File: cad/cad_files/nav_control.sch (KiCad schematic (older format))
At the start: 10 parts

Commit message: Adding refdes details for nav_control
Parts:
- gave numbers to parts that had none: 10
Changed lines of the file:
@@
-EESchema Schematic File Version 2  date Wed 03 Dec 2014 01:00:34 PM HST
+EESchema Schematic File Version 2  date Wed 03 Dec 2014 04:59:28 PM HST
 LIBS:local_parts
 LIBS:power
@@
 Sheet 2 4
 Title ""
-Date "3 dec 2014"
+Date "4 dec 2014"
 Rev ""
 Comp ""
@@
 charge_status
 $Comp
-L ARDUINO_PRO_MINI U?
+L ARDUINO_PRO_MINI Uc101
 U 1 1 547EB67E
 P 3000 5000
-F 0 "U?" H 3000 4900 50  0000 C CNN
+F 0 "Uc101" H 3000 4900 50  0000 C CNN
 F 1 "ARDUINO_PRO_MINI" V 3100 5350 50  0000 C CNN
 F 2 "MODULE" H 3000 5000 50  0001 C CNN
@@
 $EndComp
 $Comp
-L R R?
+L R Rc101
 U 1 1 547E9539
 P 2900 3550
-F 0 "R?" V 2980 3550 50  0000 C CNN
+F 0 "Rc101" V 2980 3550 50  0000 C CNN
 F 1 "DNP" V 2900 3550 50  0000 C CNN
 	1    2900 3550
@@
 for power switching \nbypass (always on)
 $Comp
-L R R?
+L R Rp303
 U 1 1 547C6270
 P 5100 1800
-F 0 "R?" V 5180 1800 50  0000 C CNN
+F 0 "Rp303" V 5180 1800 50  0000 C CNN
 F 1 "DNP" V 5100 1800 50  0000 C CNN
 	1    5100 1800
@@
 header for power supply \n(boost  to 3.3 or 5 V)\ncheck rotation...
 $Comp
-L CONN_3 K?
+L CONN_3 Kp301
 U 1 1 546DDB52
 P 6350 2500
-F 0 "K?" V 6300 2500 50  0000 C CNN
+F 0 "Kp301" V 6300 2500 50  0000 C CNN
 F 1 "CONN_3" V 6400 2500 40  0000 C CNN
 	1    6350 2500
@@
 Vppath
 $Comp
-L MOSFET_P Q?
+L MOSFET_P Qp301
 U 1 1 53D1B1AA
 P 4700 1800
-F 0 "Q?" H 4700 1990 60  0000 R CNN
+F 0 "Qp301" H 4700 1990 60  0000 R CNN
 F 1 "MOSFET_P" H 4700 1620 60  0000 R CNN
 	1    4700 1800
@@
 $EndComp
 $Comp
-L DIODE D?
+L DIODE Dp301
 U 1 1 53D1B1A5
 P 3700 1200
-F 0 "D?" H 3700 1300 40  0000 C CNN
+F 0 "Dp301" H 3700 1300 40  0000 C CNN
 F 1 "DIODE" H 3700 1100 40  0000 C CNN
 	1    3700 1200
@@
 $EndComp
 $Comp
-L DIODE D?
+L DIODE Dp302
 U 1 1 53D1B19F
 P 3700 1600
-F 0 "D?" H 3700 1700 40  0000 C CNN
+F 0 "Dp302" H 3700 1700 40  0000 C CNN
 F 1 "DIODE" H 3700 1500 40  0000 C CNN
 	1    3700 1600
@@
 $EndComp
 $Comp
-L R R?
+L R Rp302
 U 1 1 53D1B197
 P 4100 2250
-F 0 "R?" V 4180 2250 50  0000 C CNN
+F 0 "Rp302" V 4180 2250 50  0000 C CNN
 F 1 "R" V 4100 2250 50  0000 C CNN
 	1    4100 2250
@@
 $EndComp
 $Comp
-L R R?
+L R Rp301
 U 1 1 53D1B192
 P 3300 2250
-F 0 "R?" V 3380 2250 50  0000 C CNN
+F 0 "Rp301" V 3380 2250 50  0000 C CNN
 F 1 "R" V 3300 2250 50  0000 C CNN
 	1    3300 2250
@@
 $EndComp
 $Comp
-L SW_PUSH SW?
+L SW_PUSH SWp301
 U 1 1 53D1B188
 P 2800 1800
-F 0 "SW?" H 2950 1910 50  0000 C CNN
+F 0 "SWp301" H 2950 1910 50  0000 C CNN
 F 1 "SW_PUSH" H 2800 1720 50  0000 C CNN
 	1    2800 1800

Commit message: Changing transistor to load switch for soft power
FPF2103 or a related model
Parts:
- removed Qp301: MOSFET_P, symbol MOSFET_P
- added Up301: FPF2100, symbol FPF2100
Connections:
- net labels added: PWR_FAULT
- wire segments 39 -> 45
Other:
- moved on the sheet: Kp301, Rp303
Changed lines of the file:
@@
-EESchema Schematic File Version 2  date Wed 03 Dec 2014 04:59:28 PM HST
+EESchema Schematic File Version 2  date Wed 03 Dec 2014 05:34:03 PM HST
 LIBS:local_parts
 LIBS:power
@@
 Comment4 ""
 $EndDescr
-Connection ~ 5900 2200
-Wire Wire Line
-	5900 2200 5900 2400
+Wire Wire Line
+	5500 2600 5600 2600
+Wire Wire Line
+	4500 2500 4500 2400
+Wire Wire Line
+	4500 2400 4600 2400
+Wire Wire Line
+	4600 2600 4300 2600
+Wire Wire Line
+	4300 2600 4300 1800
+Connection ~ 6200 2200
+Wire Wire Line
+	6200 2200 6200 2000
+Wire Wire Line
+	3800 4800 4000 4800
+Wire Wire Line
+	3800 4500 4000 4500
+Connection ~ 3100 6200
+Wire Wire Line
+	3100 6200 3200 6200
+Wire Wire Line
+	3200 6200 3200 6100
+Wire Wire Line
+	2700 3300 2700 3900
+Wire Wire Line
+	2900 3200 2900 3300
+Wire Wire Line
+	6500 2500 6200 2500
+Wire Wire Line
+	6200 2500 6200 2400
+Connection ~ 2300 1000
+Wire Wire Line
+	2500 1000 5600 1000
+Connection ~ 5600 2200
+Wire Wire Line
+	5600 2050 5600 2200
+Wire Wire Line
+	4100 2700 4100 2500
+Wire Wire Line
+	2500 1800 2300 1800
+Wire Wire Line
+	2300 1800 2300 1000
+Connection ~ 4100 1800
+Wire Wire Line
+	4300 1800 4100 1800
+Wire Wire Line
+	3300 1200 3500 1200
+Connection ~ 3300 1600
+Wire Wire Line
+	3500 1600 3300 1600
+Wire Wire Line
+	3300 2000 3300 1400
+Wire Wire Line
+	3100 1800 3300 1800
+Connection ~ 3300 1800
+Wire Wire Line
+	3900 1600 4100 1600
+Wire Wire Line
+	3900 1200 4100 1200
+Wire Wire Line
+	4100 1200 4100 2000
+Connection ~ 4100 1600
+Wire Wire Line
+	4500 1000 4500 2200
+Wire Wire Line
+	3300 2500 3300 2600
+Wire Wire Line
+	3300 2600 4100 2600
+Connection ~ 4100 2600
+Wire Wire Line
+	5600 1000 5600 1550
+Connection ~ 4500 1000
+Wire Wire Line
+	2000 1100 2200 1100
+Wire Wire Line
+	2200 1100 2200 1300
+Wire Wire Line
+	7100 2200 5500 2200
+Wire Wire Line
+	6500 2400 6400 2400
+Wire Wire Line
+	6500 2600 6400 2600
+Wire Wire Line
+	6400 2600 6400 2700
+Wire Wire Line
+	2900 3900 2900 3800
+Wire Wire Line
+	3100 6100 3100 6300
+Wire Wire Line
+	3800 4400 4000 4400
+Wire Wire Line
+	3800 4600 4000 4600
 Wire Wire Line
 	3800 4900 4000 4900
 Wire Wire Line
-	3800 4600 4000 4600
-Wire Wire Line
-	3800 4400 4000 4400
-Wire Wire Line
-	3100 6100 3100 6300
-Wire Wire Line
-	2900 3900 2900 3800
-Wire Wire Line
-	5900 2700 5900 2600
-Wire Wire Line
-	5900 2600 6000 2600
-Wire Wire Line
-	5900 2400 6000 2400
-Wire Wire Line
-	6600 2200 4800 2200
-Wire Wire Line
-	2200 1300 2200 1100
-Wire Wire Line
-	2200 1100 2000 1100
-Connection ~ 4800 1000
-Wire Wire Line
-	5100 1550 5100 1000
-Connection ~ 4100 2600
-Wire Wire Line
-	4100 2600 3300 2600
-Wire Wire Line
-	3300 2600 3300 2500
-Wire Wire Line
-	4800 1600 4800 1000
-Wire Wire Line
-	4800 2200 4800 2000
-Connection ~ 4100 1600
-Wire Wire Line
-	4100 2000 4100 1200
-Wire Wire Line
-	4100 1200 3900 1200
-Wire Wire Line
-	3900 1600 4100 1600
-Connection ~ 3300 1800
-Wire Wire Line
-	3100 1800 3300 1800
-Wire Wire Line
-	3300 2000 3300 1400
-Wire Wire Line
-	3300 1600 3500 1600
-Connection ~ 3300 1600
-Wire Wire Line
-	3300 1200 3500 1200
-Wire Wire Line
-	4100 1800 4500 1800
-Connection ~ 4100 1800
-Wire Wire Line
-	2300 1000 2300 1800
-Wire Wire Line
-	2300 1800 2500 1800
-Wire Wire Line
-	4100 2700 4100 2500
-Wire Wire Line
-	5100 2050 5100 2200
-Connection ~ 5100 2200
-Wire Wire Line
-	5100 1000 2000 1000
-Connection ~ 2300 1000
-Wire Wire Line
-	5700 2400 5700 2500
-Wire Wire Line
-	5700 2500 6000 2500
-Wire Wire Line
-	2900 3200 2900 3300
-Wire Wire Line
-	2700 3300 2700 3900
-Wire Wire Line
-	3200 6100 3200 6200
-Wire Wire Line
-	3200 6200 3100 6200
-Connection ~ 3100 6200
-Wire Wire Line
-	3800 4500 4000 4500
-Wire Wire Line
-	3800 4800 4000 4800
-Wire Wire Line
-	5700 2000 5700 2200
-Connection ~ 5700 2200
+	6400 2400 6400 2200
+Connection ~ 6400 2200
+Wire Wire Line
+	4500 2200 4600 2200
+Wire Wire Line
+	3800 5000 4000 5000
+Text Label 5600 2600 0    60   ~ 0
+PWR_FAULT
+Text Label 4000 5000 0    60   ~ 0
+PWR_FAULT
+$Comp
+L GND #PWR?
+U 1 1 547FD4F0
+P 4500 2500
+F 0 "#PWR?" H 4500 2500 30  0001 C CNN
+F 1 "GND" H 4500 2430 30  0001 C CNN
+	1    4500 2500
+	1    0    0    -1
+$EndComp
+$Comp
+L FPF2100 Up301
+U 1 1 547FD495
+P 5050 2400
+F 0 "Up301" H 5050 2300 60  0000 C CNN
+F 1 "FPF2100" H 5050 2500 60  0000 C CNN
+	1    5050 2400
+	1    0    0    -1
+$EndComp
 Text Notes 4900 4800 0    60   ~ 0
 P6 to turn on LED (PWM: 3, 5, 6, 9, 10, 11)\nP7 to turn on  power (when running with a soft switch)
@@
 L +5V #PWR?
 U 1 1 547E62DF
-P 5700 2400
-F 0 "#PWR?" H 5700 2490 20  0001 C CNN
-F 1 "+5V" H 5700 2490 30  0000 C CNN
-	1    5700 2400
+P 6200 2400
+F 0 "#PWR?" H 6200 2490 20  0001 C CNN
+F 1 "+5V" H 6200 2490 30  0000 C CNN
+	1    6200 2400
 	1    0    0    -1
 $EndComp
@@
 L GND #PWR?
 U 1 1 547E62B9
-P 5900 2700
-F 0 "#PWR?" H 5900 2700 30  0001 C CNN
-F 1 "GND" H 5900 2630 30  0001 C CNN
-	1    5900 2700
+P 6400 2700
+F 0 "#PWR?" H 6400 2700 30  0001 C CNN
+F 1 "GND" H 6400 2630 30  0001 C CNN
+	1    6400 2700
 	1    0    0    -1
 $EndComp
@@
 	1    0    0    -1
 $EndComp
-Text HLabel 6600 2200 2    60   Input ~ 0
+Text HLabel 7100 2200 2    60   Input ~ 0
 powerpath_vdd
 Text HLabel 4000 4600 2    60   Input ~ 0
@@
 Text HLabel 2000 1000 0    60   Input ~ 0
 battery_pos
-Text Notes 6500 2450 0    60   ~ 0
+Text Notes 7000 2450 0    60   ~ 0
 Vbat\n+5V\nGND
-Text Notes 5300 1700 0    60   ~ 0
+Text Notes 5800 1700 0    60   ~ 0
 for power switching \nbypass (always on)
 $Comp
 L R Rp303
 U 1 1 547C6270
-P 5100 1800
-F 0 "Rp303" V 5180 1800 50  0000 C CNN
-F 1 "DNP" V 5100 1800 50  0000 C CNN
-	1    5100 1800
-	1    0    0    -1
-$EndComp
-Text Notes 6000 2800 0    60   ~ 0
+P 5600 1800
+F 0 "Rp303" V 5680 1800 50  0000 C CNN
+F 1 "DNP" V 5600 1800 50  0000 C CNN
+	1    5600 1800
+	1    0    0    -1
+$EndComp
+Text Notes 6500 2800 0    60   ~ 0
 header for power supply \n(boost  to 3.3 or 5 V)\ncheck rotation...
 $Comp
 L CONN_3 Kp301
 U 1 1 546DDB52
-P 6350 2500
-F 0 "Kp301" V 6300 2500 50  0000 C CNN
-F 1 "CONN_3" V 6400 2500 40  0000 C CNN
-	1    6350 2500
+P 6850 2500
+F 0 "Kp301" V 6800 2500 50  0000 C CNN
+F 1 "CONN_3" V 6900 2500 40  0000 C CNN
+	1    6850 2500
 	1    0    0    -1
 $EndComp
@@
 Text Label 3300 1200 2    60   ~ 0
 uC_PWR_CTRL
-Text Label 5700 2000 0    60   ~ 0
+Text Label 6200 2000 0    60   ~ 0
 Vppath
 $Comp
-L MOSFET_P Qp301
-U 1 1 53D1B1AA
-P 4700 1800
-F 0 "Qp301" H 4700 1990 60  0000 R CNN
-F 1 "MOSFET_P" H 4700 1620 60  0000 R CNN
-	1    4700 1800
-	1    0    0    -1
-$EndComp
-$Comp
 L DIODE Dp301

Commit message: ERC clearing
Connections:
- wire segments 45 -> 49
- no-connect marks 0 -> 18
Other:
- moved on the sheet: Kp301, Rc101
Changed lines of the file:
@@
-EESchema Schematic File Version 2  date Wed 03 Dec 2014 05:36:52 PM HST
+EESchema Schematic File Version 2  date Wed 03 Dec 2014 05:46:12 PM HST
 LIBS:local_parts
 LIBS:power
@@
 Comment4 ""
 $EndDescr
+Connection ~ 2200 1100
+Wire Wire Line
+	2200 800  2200 1300
+Connection ~ 6400 2600
+Wire Wire Line
+	6700 2600 6200 2600
+Wire Wire Line
+	6200 2600 6200 2500
+Wire Wire Line
+	3800 5000 4000 5000
+Wire Wire Line
+	4600 2200 4500 2200
+Connection ~ 6600 2200
+Wire Wire Line
+	6600 2500 6600 2200
+Wire Wire Line
+	3800 4900 4000 4900
+Wire Wire Line
+	3800 4600 4000 4600
+Wire Wire Line
+	3800 4400 4000 4400
+Wire Wire Line
+	3100 6100 3100 6300
+Wire Wire Line
+	2900 3900 2900 3700
+Wire Wire Line
+	6600 2800 6600 2700
+Wire Wire Line
+	6600 2700 6700 2700
+Wire Wire Line
+	6600 2500 6700 2500
+Wire Wire Line
+	7100 2200 5500 2200
+Wire Wire Line
+	2200 1100 2000 1100
+Connection ~ 4500 1000
+Wire Wire Line
+	5600 1000 5600 1550
+Connection ~ 4100 2600
+Wire Wire Line
+	3300 2600 4100 2600
+Wire Wire Line
+	3300 2600 3300 2500
+Wire Wire Line
+	4500 2200 4500 1000
+Connection ~ 4100 1600
+Wire Wire Line
+	4100 2000 4100 1200
+Wire Wire Line
+	4100 1200 3900 1200
+Wire Wire Line
+	3900 1600 4100 1600
+Connection ~ 3300 1800
+Wire Wire Line
+	3100 1800 3300 1800
+Wire Wire Line
+	3300 2000 3300 1400
+Wire Wire Line
+	3300 1600 3500 1600
+Connection ~ 3300 1600
+Wire Wire Line
+	3300 1200 3500 1200
+Wire Wire Line
+	4100 1800 4300 1800
+Connection ~ 4100 1800
+Wire Wire Line
+	2300 1000 2300 1800
+Wire Wire Line
+	2300 1800 2500 1800
+Wire Wire Line
+	4100 2700 4100 2500
+Wire Wire Line
+	5600 2200 5600 2050
+Connection ~ 5600 2200
+Wire Wire Line
+	2000 1000 5600 1000
+Connection ~ 2300 1000
+Wire Wire Line
+	6400 2500 6400 2600
+Wire Wire Line
+	2900 3100 2900 3200
+Wire Wire Line
+	2700 3300 2700 3900
+Wire Wire Line
+	3200 6100 3200 6200
+Wire Wire Line
+	3200 6200 3100 6200
+Connection ~ 3100 6200
+Wire Wire Line
+	3800 4500 4000 4500
+Wire Wire Line
+	3800 4800 4000 4800
+Wire Wire Line
+	6400 2200 6400 2000
+Connection ~ 6400 2200
+Wire Wire Line
+	4300 1800 4300 2600
+Wire Wire Line
+	4300 2600 4600 2600
+Wire Wire Line
+	4600 2400 4500 2400
+Wire Wire Line
+	4500 2400 4500 2500
 Wire Wire Line
 	5500 2600 5600 2600
 Wire Wire Line
-	4500 2500 4500 2400
-Wire Wire Line
-	4500 2400 4600 2400
-Wire Wire Line
-	4600 2600 4300 2600
-Wire Wire Line
-	4300 2600 4300 1800
-Connection ~ 6200 2200
-Wire Wire Line
-	6200 2200 6200 2000
-Wire Wire Line
-	3800 4800 4000 4800
-Wire Wire Line
-	3800 4500 4000 4500
-Connection ~ 3100 6200
-Wire Wire Line
-	3100 6200 3200 6200
-Wire Wire Line
-	3200 6200 3200 6100
-Wire Wire Line
-	2700 3300 2700 3900
-Wire Wire Line
-	2900 3200 2900 3300
-Wire Wire Line
-	6500 2500 6200 2500
-Wire Wire Line
-	6200 2500 6200 2400
-Connection ~ 2300 1000
-Wire Wire Line
-	2500 1000 5600 1000
-Connection ~ 5600 2200
-Wire Wire Line
-	5600 2050 5600 2200
-Wire Wire Line
-	4100 2700 4100 2500
-Wire Wire Line
-	2500 1800 2300 1800
-Wire Wire Line
-	2300 1800 2300 1000
-Connection ~ 4100 1800
-Wire Wire Line
-	4300 1800 4100 1800
-Wire Wire Line
-	3300 1200 3500 1200
-Connection ~ 3300 1600
-Wire Wire Line
-	3500 1600 3300 1600
-Wire Wire Line
-	3300 2000 3300 1400
-Wire Wire Line
-	3100 1800 3300 1800
-Connection ~ 3300 1800
-Wire Wire Line
-	3900 1600 4100 1600
-Wire Wire Line
-	3900 1200 4100 1200
-Wire Wire Line
-	4100 1200 4100 2000
-Connection ~ 4100 1600
-Wire Wire Line
-	4500 1000 4500 2200
-Wire Wire Line
-	3300 2500 3300 2600
-Wire Wire Line
-	3300 2600 4100 2600
-Connection ~ 4100 2600
-Wire Wire Line
-	5600 1000 5600 1550
-Connection ~ 4500 1000
-Wire Wire Line
-	2000 1100 2200 1100
-Wire Wire Line
-	2200 1100 2200 1300
-Wire Wire Line
-	7100 2200 5500 2200
-Wire Wire Line
-	6500 2400 6400 2400
-Wire Wire Line
-	6500 2600 6400 2600
-Wire Wire Line
-	6400 2600 6400 2700
-Wire Wire Line
-	2900 3900 2900 3800
-Wire Wire Line
-	3100 6100 3100 6300
-Wire Wire Line
-	3800 4400 4000 4400
-Wire Wire Line
-	3800 4600 4000 4600
-Wire Wire Line
-	3800 4900 4000 4900
-Wire Wire Line
-	6400 2400 6400 2200
-Connection ~ 6400 2200
-Wire Wire Line
-	4500 2200 4600 2200
-Wire Wire Line
-	3800 5000 4000 5000
+	2500 1000 2500 800
+Connection ~ 2500 1000
+Wire Wire Line
+	2900 3800 3200 3800
+Wire Wire Line
+	3200 3800 3200 3700
+Connection ~ 2900 3800
+$Comp
+L PWR_FLAG #FLG01
+U 1 1 547FD8F3
+P 2200 800
+F 0 "#FLG01" H 2200 895 30  0001 C CNN
+F 1 "PWR_FLAG" H 2200 980 30  0000 C CNN
+	1    2200 800
+	1    0    0    -1
+$EndComp
+$Comp
+L PWR_FLAG #FLG02
+U 1 1 547FD8C6
+P 3200 3700
+F 0 "#FLG02" H 3200 3795 30  0001 C CNN
+F 1 "PWR_FLAG" H 3200 3880 30  0000 C CNN
+	1    3200 3700
+	1    0    0    -1
+$EndComp
+$Comp
+L PWR_FLAG #FLG03
+U 1 1 547FD79D
+P 2500 800
+F 0 "#FLG03" H 2500 895 30  0001 C CNN
+F 1 "PWR_FLAG" H 2500 980 30  0000 C CNN
+	1    2500 800
+	1    0    0    -1
+$EndComp
+$Comp
+L PWR_FLAG #FLG04
+U 1 1 547FD75C
+P 6200 2500
+F 0 "#FLG04" H 6200 2595 30  0001 C CNN
+F 1 "PWR_FLAG" H 6200 2680 30  0000 C CNN
+	1    6200 2500
+	1    0    0    -1
+$EndComp
+NoConn ~ 3800 5500
+NoConn ~ 3800 5400
+NoConn ~ 3800 5300
+NoConn ~ 3800 5200
+NoConn ~ 3800 5100
+NoConn ~ 3800 4700
+NoConn ~ 2200 5700
+NoConn ~ 2200 5600
+NoConn ~ 2200 5500
+NoConn ~ 2200 5400
+NoConn ~ 2200 5300
+NoConn ~ 2200 5200
+NoConn ~ 2200 5100
+NoConn ~ 2200 5000
+NoConn ~ 2200 4800
+NoConn ~ 2200 4700
+NoConn ~ 2200 4600
+NoConn ~ 2200 4500
 Text Label 5600 2600 0    60   ~ 0
 PWR_FAULT
@@
 PWR_FAULT
 $Comp
-L GND #PWR01
+L GND #PWR05
 U 1 1 547FD4F0
 P 4500 2500
-F 0 "#PWR01" H 4500 2500 30  0001 C CNN
+F 0 "#PWR05" H 4500 2500 30  0001 C CNN
 F 1 "GND" H 4500 2430 30  0001 C CNN
 	1    4500 2500
@@
 	1    0    0    -1
 $EndComp
-Text Label 2900 3200 1    60   ~ 0
+Text Label 2900 3100 1    60   ~ 0
 Vppath
 $Comp
-L GND #PWR02
+L GND #PWR06
 U 1 1 547E9671
 P 3100 6300
-F 0 "#PWR02" H 3100 6300 30  0001 C CNN
+F 0 "#PWR06" H 3100 6300 30  0001 C CNN
 F 1 "GND" H 3100 6230 30  0001 C CNN
 	1    3100 6300
@@
 L R Rc101
 U 1 1 547E9539
-P 2900 3550
-F 0 "Rc101" V 2980 3550 50  0000 C CNN
-F 1 "DNP" V 2900 3550 50  0000 C CNN
-	1    2900 3550
-	1    0    0    -1
-$EndComp
-$Comp
-L +5V #PWR03
+P 2900 3450
+F 0 "Rc101" V 2980 3450 50  0000 C CNN
+F 1 "DNP" V 2900 3450 50  0000 C CNN
+	1    2900 3450
+	1    0    0    -1
+$EndComp
+$Comp
+L +5V #PWR07
 U 1 1 547E94E8
 P 2700 3300
-F 0 "#PWR03" H 2700 3390 20  0001 C CNN
+F 0 "#PWR07" H 2700 3390 20  0001 C CNN
 F 1 "+5V" H 2700 3390 30  0000 C CNN
 	1    2700 3300
@@
 $EndComp
 $Comp
-L +5V #PWR04
+L +5V #PWR08
 U 1 1 547E62DF
-P 6200 2400
-F 0 "#PWR04" H 6200 2490 20  0001 C CNN
-F 1 "+5V" H 6200 2490 30  0000 C CNN
-	1    6200 2400
-	1    0    0    -1
-$EndComp
-$Comp
-L GND #PWR05
+P 6400 2500
+F 0 "#PWR08" H 6400 2590 20  0001 C CNN
+F 1 "+5V" H 6400 2590 30  0000 C CNN
+	1    6400 2500
+	1    0    0    -1
+$EndComp
+$Comp
+L GND #PWR09
 U 1 1 547E62B9
-P 6400 2700
-F 0 "#PWR05" H 6400 2700 30  0001 C CNN
-F 1 "GND" H 6400 2630 30  0001 C CNN
-	1    6400 2700
+P 6600 2800
+F 0 "#PWR09" H 6600 2800 30  0001 C CNN
+F 1 "GND" H 6600 2730 30  0001 C CNN
+	1    6600 2800
 	1    0    0    -1
 $EndComp
@@
 switch_control
 $Comp
-L GND #PWR06
+L GND #PWR010
 U 1 1 547DAB88
 P 2200 1300
-F 0 "#PWR06" H 2200 1300 30  0001 C CNN
+F 0 "#PWR010" H 2200 1300 30  0001 C CNN
 F 1 "GND" H 2200 1230 30  0001 C CNN
 	1    2200 1300
@@
 Text HLabel 2000 1000 0    60   Input ~ 0
 battery_pos
-Text Notes 7000 2450 0    60   ~ 0
+Text Notes 7200 2550 0    60   ~ 0
 Vbat\n+5V\nGND
 Text Notes 5800 1700 0    60   ~ 0
@@
 	1    0    0    -1
 $EndComp
-Text Notes 6500 2800 0    60   ~ 0
+Text Notes 6700 2900 0    60   ~ 0
 header for power supply \n(boost  to 3.3 or 5 V)\ncheck rotation...
 $Comp
 L CONN_3 Kp301
 U 1 1 546DDB52
-P 6850 2500
-F 0 "Kp301" V 6800 2500 50  0000 C CNN
-F 1 "CONN_3" V 6900 2500 40  0000 C CNN
-	1    6850 2500
+P 7050 2600
+F 0 "Kp301" V 7000 2600 50  0000 C CNN
+F 1 "CONN_3" V 7100 2600 40  0000 C CNN
+	1    7050 2600
 	1    0    0    -1
 $EndComp
@@
 P2 (INT0) for power button sensing\nP3 (INT1) for charger status sensing\nP4 for led status sensing (polled)
 $Comp
-L GND #PWR07
+L GND #PWR011
 U 1 1 53DB8078
 P 4100 2700
-F 0 "#PWR07" H 4100 2700 30  0001 C CNN
+F 0 "#PWR011" H 4100 2700 30  0001 C CNN
 F 1 "GND" H 4100 2630 30  0001 C CNN
 	1    4100 2700
@@
 Text Label 3300 1200 2    60   ~ 0
 uC_PWR_CTRL
-Text Label 6200 2000 0    60   ~ 0
+Text Label 6400 2000 0    60   ~ 0
 Vppath
 $Comp

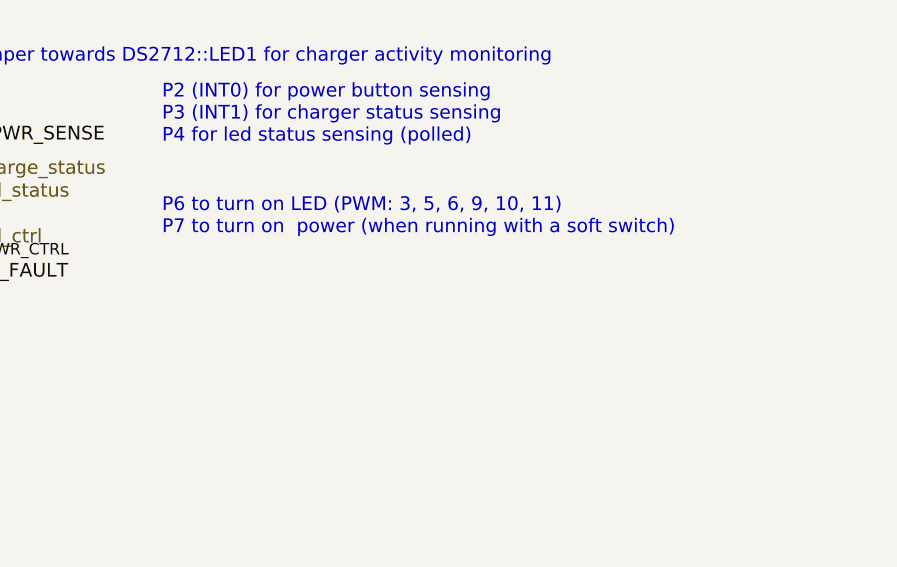
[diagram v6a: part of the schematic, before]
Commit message: Prep for layout
add footprints, refine design
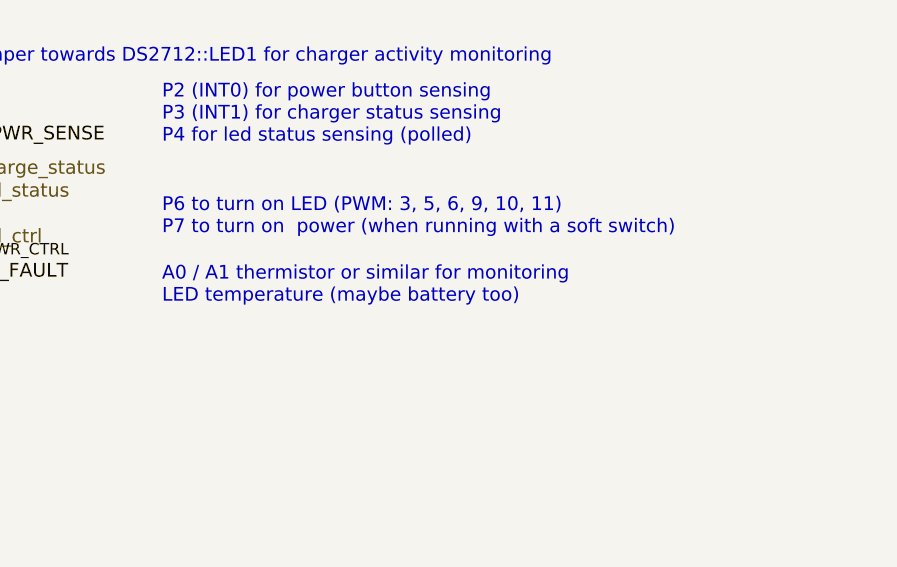
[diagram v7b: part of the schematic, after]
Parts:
- Kp301: footprint (none) -> PIN_ARRAY_3X1
- Rc101, Rp301, Rp302, Rp303: footprint (none) -> SM0805
- Uc101: footprint MODULE -> DIP-24__600_ELL
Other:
- note added: "A0 / A1 thermistor or similar for monitoring \nLED temperature (maybe battery too)"
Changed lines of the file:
@@
-EESchema Schematic File Version 2  date Wed 03 Dec 2014 05:46:12 PM HST
+EESchema Schematic File Version 2  date Sun 07 Dec 2014 02:35:16 AM HST
 LIBS:local_parts
 LIBS:power
@@
 Sheet 2 4
 Title ""
-Date "4 dec 2014"
+Date "7 dec 2014"
 Rev ""
 Comp ""
@@
 Comment4 ""
 $EndDescr
+Text Notes 4900 5100 0    60   ~ 0
+A0 / A1 thermistor or similar for monitoring \nLED temperature (maybe battery too)
 Connection ~ 2200 1100
 Wire Wire Line
@@
 F 0 "Uc101" H 3000 4900 50  0000 C CNN
 F 1 "ARDUINO_PRO_MINI" V 3100 5350 50  0000 C CNN
-F 2 "MODULE" H 3000 5000 50  0001 C CNN
+F 2 "DIP-24__600_ELL" H 3000 5000 50  0001 C CNN
 F 3 "DOCUMENTATION" H 3000 5000 50  0001 C CNN
 	1    3000 5000
@@
 F 0 "Rc101" V 2980 3450 50  0000 C CNN
 F 1 "DNP" V 2900 3450 50  0000 C CNN
+F 2 "SM0805" H 2900 3450 60  0001 C CNN
 	1    2900 3450
 	1    0    0    -1
@@
 F 0 "Rp303" V 5680 1800 50  0000 C CNN
 F 1 "DNP" V 5600 1800 50  0000 C CNN
+F 2 "SM0805" H 5600 1800 60  0001 C CNN
 	1    5600 1800
 	1    0    0    -1
@@
 F 0 "Kp301" V 7000 2600 50  0000 C CNN
 F 1 "CONN_3" V 7100 2600 40  0000 C CNN
+F 2 "PIN_ARRAY_3X1" H 7050 2600 60  0001 C CNN
 	1    7050 2600
 	1    0    0    -1
@@
 F 0 "Rp302" V 4180 2250 50  0000 C CNN
 F 1 "R" V 4100 2250 50  0000 C CNN
+F 2 "SM0805" H 4100 2250 60  0001 C CNN
 	1    4100 2250
 	1    0    0    -1
@@
 F 0 "Rp301" V 3380 2250 50  0000 C CNN
 F 1 "R" V 3300 2250 50  0000 C CNN
+F 2 "SM0805" H 3300 2250 60  0001 C CNN
 	1    3300 2250
 	1    0    0    -1
